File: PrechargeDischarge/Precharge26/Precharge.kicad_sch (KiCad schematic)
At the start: 117 parts, among them J1 MicroFit, J2 Mini-Fit_Jr_5566-04A, J3 Micro-Fit 43045-0212, K1 OMRON-G2RL-24, K2 G7L-2A-X-L, K3 Relay_SPST-NC, Q1 2N7002, Q2 MMBT3906, Q3 2N7002, Q4 PMOS, U1 TJA1051T-3, U10 LM393, U11 4N35, U2 SPAN02A-12, U3 Teensy4.0, U4 LM1117-5.0, U5 4N35, U6 4N35, U7 LM331, U8 LM331, U9 LM2904

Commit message: Precharge
Fixed Ground plane distance, added new DC converter, fixed precharge resistor value
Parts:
- R46: value HSA25390RJ -> HSA253K3J
- R51: footprint (none) -> Resistor_SMD:R_1206_3216Metric
- U2: footprint Precharge:SPAN02 -> Precharge:DC-DCSPAN02W8-12
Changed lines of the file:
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@@
 			"AEQAcgA0AGkAaQBXAEwAMwBlAFEAMgBSADQAQgBKAHQATQB5AGgAbABGAFIAcQBsAEMAbwBjAEEA"
 			"QwBQAHAALwBQAGEARABRAEsAZwBuAEQAeAA0AHMAWABTADAAbABMAGsAbQBBAEwAWABPAFgAUgA3"
-			"AG4AZQBGAHcATwBJAHEATABpAC8AMQArAFAAegBRAC8AZAByADEAQwAxAGQAaA=="
+			"AG4AZQBGAHcATwBJAHEATABpAC8AMQArAFAAegBRAC8AZAByADEAQwAxAGQAaABEADMASABPAHEA"
+			"QgBZAEYAQQBBAE8ASAB2AE0AMgBmAE8ASgBDAFEAawBEAEIANAA4AHUARgBlAHYAWABxAEkAbwBH"
+			"AG8AMQBHAHgASwA5AGgANABvAGcAMAB1ACsAcgBhAGEASAAwAEIAbQBlAEIAbwBOAEIAcgBvAGYA"
+			"eQBoAFgAKwB1AHkAegB6ACsAYgBNAG0AUwBPAEsAbwBzAGYAagBPAFgAcgAwADYAQgBOAFAAUABC"
+			"AEUAVABFADEATwBOAHgAQQA2ADAAcABxAFMAawBKAEIAZwBNAHkAbABYAG4AeABoAGEAaQBsAFMA"
+			"UQBwAE8AVABuAFoAWQBEAEMAMABhAHQAWABLAFkAcgBFAEkAZwByAEIALwAvAC8ANQBWAHEAMQBi"
+			"AGwANQBPAFEARQBnADgARwBSAEkAMABkAE8AbQBEAEEAQgBoAFYAegB2AHYALwA5ACsAUQBrAEwA"
+			"QwBMAGIAZgBjAFkAagBRAGEAVgA2ADUAYwBHAFIATQBUAE0AMgBUAEkAawBNADIAYgBOACsALwBl"
+			"AHYAUgB2AFAAagBpAEEASQBCAG8ATgBoADcATgBpAHgAVgBxAHMAVgBmAHEAaQAxAGYAWABBAGMA"
+			"agBRADYATgBiAHUAYgBIAHcAYwBGAHgALwBVAEcAeQBpAHIAeAA1AFQAUABXAHUASAA1AFgAUgBV"
+			"AE4AUwB5AHMAcgBLAG0AVABKAGsAeQBiAHQAeQA0AEkAMABlAE8AMABNAGkAcQBWAHEAdQBSAFcA"
+			"TgBZAEkAeAAxAG8AcQBpAEwASABaAGIARgBSADEAegBoAGgAVABxAFYAUwBEAEIAZwAxAGEAdAAy"
+			"ADUAZABjAG4ASgB5AFIAawBZAEcAegBOAEsAcgBsADkAVwBGAFEAcQBHAEwARgB5ADkAQwA2AEsA"
+			"MwAyAC8ASQBUADYAQQBrAEUAUQB4AG8AOABmAGIANwBGAFkAUgBvAHcAWQBFAFIAOABmAGYAKwA3"
+			"AGMAdQBWAG0AegBaAGgAMAA2AGQASwBoAEQAaAB3ADYATQBzAFoAZABmAGYAbgBuADcAOQB1ADAA"
+			"NABNADYAdABXAHIAZABxAHcAWQBZAFAASAA0ADUARQBrAGEAZQBYAEsAbABkADkAKwArACsAMgA1"
+			"AGMAKwBkAE8AbgB6ADYAZABrADUAUAB6AHcAUQBjAGYATABGADIANgA5AEsATwBQAFAAdABxAHkA"
+			"WgBZAHYAUAA1ADQAUABvAGkATQBsAFMAYgBSADgAZgBSACsATQBDAEoANAA0AGMASABCAHcAMQBE"
+			"AGoAQQBWAHAAVgBLAEoAVQBEAFgAVgBvADEAUQBYAHcASABXAGcAYQBQAHIAOQ=="
 		)
 	)
@@
 			)
 		)
-		(property "Footprint" "Precharge:SPAN02"
+		(property "Footprint" "Precharge:DC-DCSPAN02W8-12"
 			(at 62.23 135.89 0)
 			(effects
@@
 			)
 		)
-		(property "Value" "HSA25390RJ"
+		(property "Value" "HSA253K3J"
 			(at 63.5 213.36 90)
 			(effects
@@
 			)
 		)
-		(property "Footprint" ""
+		(property "Footprint" "Resistor_SMD:R_1206_3216Metric"
 			(at 65.786 45.974 90)
 			(effects

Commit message: added discharge relay and resistor footprints to precharge board
still need all part numbers but ffootprints are selected, go shopping on JLC
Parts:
- removed K3: Relay_SPST-NC, Library:Relay_SPST_NC_COMUS, symbol Relay:Relay_SPST-NC
- removed Q4: PMOS, Package_TO_SOT_THT:TO-220-3_Vertical, symbol Simulation_SPICE:PMOS
- added D13: D, Diode_SMD:D_SMA, symbol Device:D
- added H1: MountingHole, MountingHole:MountingHole_3.2mm_M3, symbol Mechanical:MountingHole
- added H2: MountingHole, symbol Mechanical:MountingHole
- added J4: Micro-Fit 43045-0212, Connector_Molex:Molex_Micro-Fit_3.0_43045-0212_2x01_P3.00mm_Vertical, symbol Connector:Conn_01x02_Pin
- added K4: Relay_SPST-NC, Precharge:Discharge_relay, symbol Relay:SANYOU_SRD_Form_C
- added Q5: NMOS, Package_TO_SOT_SMD:SOT-23, symbol Simulation_SPICE:NMOS
- J1: symbol Connector:Conn_01x08_Female -> Connector:Conn_01x08_Pin
- J2: symbol Connector:Conn_01x04_Female -> Connector:Conn_01x04_Pin
- J3: symbol Connector:Conn_01x02_Female -> Connector:Conn_01x02_Pin
- R50: value 3k -> HSA503K0J; footprint (none) -> Precharge:Discharge_Resistor
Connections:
- net SHUTDOWN is gone; now on net GLV+: R51.1
- net +12V: now also D13.1 (K), K4.2
- net CANH: now also J1.8 (Pin_8)
- net CANL: now also J1.7 (Pin_7)
- net GLV+: now also J1.1 (Pin_1), Q5.2 (G)
- net GLV-: now also J1.5 (Pin_5), Q5.3 (S)
- net PDOC_OK: now also J1.6 (Pin_6)
- net PRECH_STS: now also J1.4 (Pin_4)
- net SHTDN_OUT: now also J1.3 (Pin_3)
- net TS-: now also J3.1 (Pin_1), J3.2 (Pin_2)
- net VinTS: now also J2.4 (Pin_4)
- net at K2.8: now also J2.1 (Pin_1)
- net at R50.1: now also K4.4
- net HV_OUT renamed MSD_IN
- net MSD_IN: now also J4.2 (Pin_2)
- new net: D13.2 (A), K4.5, Q5.1 (D)
- new net IR+_MC: J4.1 (Pin_1), K4.1
- no-connect marks 9 -> 12
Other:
- note added: "voltage of the shutdown circuit. 12V when on, 0V when off, want discharge to be open when shutdown circuit is 12V"
- note removed: "SHUTDOWN is the voltage of the shutdown circui. 12V when on, 0V when off"
- moved on the sheet: R51

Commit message: precharge
fixed board edges
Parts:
- K1: JLC (none) -> C1524522; MFR (none) -> G2RL-24 DC12

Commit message: precharge/discharge. charging
removed discharge ffrom precharge and put it on board out of battery, updqted charging according to discharge
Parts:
- removed H1: MountingHole, MountingHole:MountingHole_3.2mm_M3, symbol Mechanical:MountingHole
- removed H2: MountingHole, symbol Mechanical:MountingHole
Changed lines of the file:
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@@
 	(text_box "PRECHARGE"
 		(exclude_from_sim no)
-		(at 11.43 111.76 0)
+		(at -132.08 170.18 0)
 		(size 426.72 289.56)
 		(margins 0.9525 0.9525 0.9525 0.9525)
@@
 				)
 				(justify left)
+				(hide yes)
 			)
 		)
@@
 				)
 				(justify left)
+				(hide yes)
 			)
 		)
@@
 					(size 1.27 1.27)
 				)
+				(hide yes)
 			)
 		)
@@
 	)
 	(symbol
-		(lib_id "Mechanical:MountingHole")
-		(at 472.44 226.06 0)
-		(unit 1)
-		(exclude_from_sim no)
-		(in_bom no)
-		(on_board yes)
-		(dnp no)
-		(fields_autoplaced yes)
-		(property "Reference" "H2"
-			(at 474.98 224.7899 0)
-			(effects
-				(font
-					(size 1.27 1.27)
-				)
-				(justify left)
-			)
-		)
-		(property "Value" "MountingHole"
-			(at 474.98 227.3299 0)
-			(effects
-				(font
-					(size 1.27 1.27)
-				)
-				(justify left)
-			)
-		)
-		(property "Footprint" ""
-			(at 472.44 226.06 0)
-			(effects
-				(font
-					(size 1.27 1.27)
-				)
-				(hide yes)
-			)
-		)
-		(property "Datasheet" "~"
-			(at 472.44 226.06 0)
-			(effects
-				(font
-					(size 1.27 1.27)
-				)
-				(hide yes)
-			)
-		)
-		(property "Description" "Mounting Hole without connection"
-			(at 472.44 226.06 0)
-			(effects
-				(font
-					(size 1.27 1.27)
-				)
-				(hide yes)
-			)
-		)
-		(property "JLC" ""
-			(at 472.44 226.06 0)
-			(effects
-				(font
-					(size 1.27 1.27)
-				)
-				(hide yes)
-			)
-		)
-		(property "MFR" ""
-			(at 472.44 226.06 0)
-			(effects
-				(font
-					(size 1.27 1.27)
-				)
-				(hide yes)
-			)
-		)
-		(instances
-			(project "Precharge"
-				(path "/56395b7f-8d0b-4695-8aad-21fefa44f8f8"
-					(reference "H2")
-					(unit 1)
-				)
-			)
-		)
-	)
-	(symbol
 		(lib_id "Simulation_SPICE:NMOS")
 		(at 101.6 59.69 90)
@@
 					(unit 1)
 				)
-			)
-		)
-	)
-	(symbol
-		(lib_id "Mechanical:MountingHole")
-		(at 472.44 218.44 0)
-		(unit 1)
-		(exclude_from_sim no)
-		(in_bom no)
-		(on_board yes)
-		(dnp no)
-		(fields_autoplaced yes)
-		(property "Reference" "H1"
-			(at 474.98 217.1699 0)
-			(effects
-				(font
-					(size 1.27 1.27)
-				)
-				(justify left)
-			)
-		)
-		(property "Value" "MountingHole"
-			(at 474.98 219.7099 0)
-			(effects
-				(font
-					(size 1.27 1.27)
-				)
-				(justify left)
-			)
-		)
-		(property "Footprint" "MountingHole:MountingHole_3.2mm_M3"
-			(at 472.44 218.44 0)
-			(effects
-				(font
-					(size 1.27 1.27)
-				)
-				(hide yes)
-			)
-		)
-		(property "Datasheet" "~"
-			(at 472.44 218.44 0)
-			(effects
-				(font
-					(size 1.27 1.27)
-				)
-				(hide yes)
-			)
-		)
-		(property "Description" "Mounting Hole without connection"
-			(at 472.44 218.44 0)
-			(effects
-				(font
-					(size 1.27 1.27)
-				)
-				(hide yes)
-			)
-		)
-		(property "JLC" ""
-			(at 472.44 218.44 0)
-			(effects
-				(font
-					(size 1.27 1.27)
-				)
-				(hide yes)
-			)
-		)
-		(property "MFR" ""
-			(at 472.44 218.44 0)
-			(effects
-				(font
-					(size 1.27 1.27)
-				)
-				(hide yes)
-			)
-		)
-		(instances
-			(project ""
-				(path "/56395b7f-8d0b-4695-8aad-21fefa44f8f8"
-					(reference "H1")
-					(unit 1)
-				)

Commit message: Molex Microfit
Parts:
- removed J3: Micro-Fit 43045-0212, Connector_Molex:Molex_Micro-Fit_3.0_43045-0212_2x01_P3.00mm_Vertical, symbol Connector:Conn_01x02_Pin
- added J3: 447690401, Precharge:MICROFIT-4PIN, symbol precharge-lib 2:447690401
- J2: footprint Mini-Fit-Jr-4.20mm-pitch:Molex-Mini-Fit-Jr-4-pin-P4.2mm-RowP4.2mm -> Precharge:MICROFIT-4PIN
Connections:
- net TS-: now also J3.1, J3.2
- no-connect marks 12 -> 14
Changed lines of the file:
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@@
 	)
 	(no_connect
+		(at 270.51 322.58)
+	)
+	(no_connect
 		(at 36.83 229.87)
 	)
@@
 	)
 	(no_connect
+		(at 270.51 325.12)
+	)
+	(no_connect
 		(at 27.94 162.56)
 	)
@@
 			"AGMAKwBkAE8AbgB6ADYAZABrADUAUAB6AHcAUQBjAGYATABGADIANgA5AEsATwBQAFAAdABxAHkA"
 			"WgBZAHYAUAA1ADQAUABvAGkATQBsAFMAYgBSADgAZgBSACsATQBDAEoANAA0AGMASABCAHcAMQBE"
-			"AGoAQQBWAHAAVgBLAEoAVQBEAFgAVgBvADEAUQBYAHcASABXAGcAYQBQAHIAOQ=="
+			"AGoAQQBWAHAAVgBLAEoAVQBEAFgAVgBvADEAUQBYAHcASABXAGcAYQBQAHIAOf/Qxaz/0MWs/9DF"
+			"rP/Qxaz/0MWs/9DFrP/Qxaz/0MWs/9DFrP/Qxaz/0MWs/9DFrP/Qxaz/0MWs/9DFrP/Qxaz/0MWs"
+			"/9DFrP/Qxaz/0MWs/9DFrP/Qxaz/0MWs/9DFrP/Qxaz/0MWs/9DFrP/Qxaz/0MWs/9DFrP/Qxaz/"
+			"0MWs/9DFrP/Qxaz/0MWs/9DFrP/Qxaz/0MWs/9DFrP/Qxaz/0MWs/9DFrP/Qxaz/0MWs/9DFrP/Q"
+			"xaz/0MWs/9DFrP/Qxaz/0MWs/9DFrP/Qxaz/0MWs/9DFrP/Qxaz/0MWs/9DFrP9+enL/VFRU/1RU"
+			"VP9UVFT/VFRU/1RUVP9UVFT/VFRU/1RUVP9UVFT/VFRU/9DFrP/Qxaz/0MWs/9DFrP/Qxaz/0MWs"
+			"/9DFrP/Qxaz/0MWs/9DFrP/Qxaz/0MWs/9DFrP/Qxaz/0MWs/9DFrP/Qxaz/0MWs/9DFrP/Qxaz/"
+			"0MWs/9DFrP/Qxaz/0MWs/9DFrP/Qxaz/0MWs/9DFrP/Qxaz/0MWs/9DFrP/Qxaz/0MWs/9DFrP/Q"
+			"xaz/0MWs/9DFrP/Qxaz/0MWs/9DFrP/Qxaz/0MWs/9DFrP/Qxaz/0MWs/9DFrP/Qxaz/0MWs/9DF"
+			"rP/Qxaz/0MWs/9DFrP/Qxaz/0MWs/9DFrP/Qxaz/0MWs/9DFrP/Qxaz/0MWs/9DFrP/Qxaz/0MWs"
+			"/9DFrP/Qxaz/0MWs/9DFrP/Qxaz/0MWs/9DFrP/Qxaz/0MWs/9DFrP/Qxaz/0MWs/9DFrP/Qxaz/"
+			"0MWs/9DFrP/Qxaz/0MWs/9DFrP/Qxaz/0MWs/9DFrP/Qxaz/0MWs/9DFrP/Qxaz/0MWs/9DFrP/Q"
+			"xaz/0MWs/9DFrP/Qxaz/0MWs/9DFrP/Qxaz/0MWs/9DFrP/Qxaz/0MWs/9DFrP/Qxaz/0MWs/9DF"
+			"rP/Qxaz/0MWs/9DFrP/Qxaz/0MWs/9DFrP/Qxaz/0MWs/9DFrP/Qxaz/0MWs/9DFrP/Qxaz/0MKq"
+			"NgAAAAAAAAAAAAAAAAAAAAAAAAAAAAAAAAAAAAAAAAAAAAAAAAAAAAAAAAAAAAAAAAAAAAAAAAAA"
+			"AAAAAAAAAAAAAAAAz8SrhdDFrP/Qxaz/0MWs/9DFrP/Qxaz/0MWs/9DFrP/Qxaz/0MWs/9DFrP/Q"
+			"xaz/0MWs/9DFrP/Qxaz/0MWs/9DFrP/Qxaz/0MWs/9DFrP/Qxaz/0MWs/9DFrP/Qxaz/0MWs/9DF"
+			"rP/Qxaz/0MWs/9DFrP/Qxaz/0MWs/9DFrP/Qxaz/0MWs/9DFrP/Qxaz/0MWs/9DFrP/Qxaz/0MWs"
+			"/9DFrP/Qxaz/0MWs/9DFrP/Qxaz/0MWs/9DFrP/Qxaz/0MWs/9DFrP/Qxaz/0A=="
 		)
 	)
@@
 	)
 	(symbol
-		(lib_id "Connector:Conn_01x02_Pin")
-		(at 275.59 317.5 0)
-		(mirror y)
-		(unit 1)
-		(exclude_from_sim no)
-		(in_bom yes)
-		(on_board yes)
-		(dnp no)
-		(property "Reference" "J3"
-			(at 278.3332 312.801 0)
-			(effects
-				(font
-					(size 1.27 1.27)
-				)
-			)
-		)
-		(property "Value" "Micro-Fit 43045-0212"
-			(at 278.3332 315.1124 0)
-			(effects
-				(font
-					(size 1.27 1.27)
-				)
-			)
-		)
-		(property "Footprint" "Connector_Molex:Molex_Micro-Fit_3.0_43045-0212_2x01_P3.00mm_Vertical"
-			(at 275.59 317.5 0)
-			(effects
-				(font
-					(size 1.27 1.27)
-				)
-				(hide yes)
-			)
-		)
-		(property "Datasheet" "~"
-			(at 275.59 317.5 0)
-			(effects
-				(font
-					(size 1.27 1.27)
-				)
-				(hide yes)
-			)
-		)
-		(property "Description" "Generic connector, single row, 01x02, script generated"
-			(at 275.59 317.5 0)
-			(effects
-				(font
-					(size 1.27 1.27)
-				)
-				(hide yes)
-			)
-		)
-		(property "JLC" ""
-			(at 275.59 317.5 0)
-			(effects
-				(font
-					(size 1.27 1.27)
-				)
-				(hide yes)
-			)
-		)
-		(property "MFR" ""
-			(at 275.59 317.5 0)
-			(effects
-				(font
-					(size 1.27 1.27)
-				)
-				(hide yes)
-			)
-		)
-		(pin "1"
-		)
-		(pin "2"
-		)
-		(instances
-			(project ""
-				(path "/56395b7f-8d0b-4695-8aad-21fefa44f8f8"
-					(reference "J3")
-					(unit 1)
-				)
-			)
-		)
-	)
-	(symbol
 		(lib_id "Isolator:4N35")
 		(at 55.88 300.99 0)
@@
 			)
 		)
-		(property "Footprint" "Mini-Fit-Jr-4.20mm-pitch:Molex-Mini-Fit-Jr-4-pin-P4.2mm-RowP4.2mm"
+		(property "Footprint" "Precharge:MICROFIT-4PIN"
 			(at 31.75 229.87 0)
 			(effects
@@
 					(unit 1)
 				)
+			)
+		)
+	)
+	(symbol
+		(lib_id "precharge-lib 2:447690401")
+		(at 270.51 317.5 0)
+		(unit 1)
+		(exclude_from_sim no)
+		(in_bom yes)
+		(on_board yes)
+		(dnp no)
+		(fields_autoplaced yes)
+		(property "Reference" "J3"
+			(at 284.48 320.0399 0)
+			(effects
+				(font
+					(size 1.524 1.524)
+				)
+				(justify left)
+			)
+		)
+		(property "Value" "447690401"
+			(at 284.48 322.5799 0)
+			(effects
+				(font
+					(size 1.524 1.524)
+				)
+				(justify left)
+			)
+		)
+		(property "Footprint" "Precharge:MICROFIT-4PIN"
+			(at 270.51 317.5 0)
+			(effects
+				(font
+					(size 1.27 1.27)
+					(italic yes)
+				)
+				(hide yes)
+			)
+		)
+		(property "Datasheet" "https://www.molex.com/en-us/products/part-detail-pdf/447690401?display=pdf"
+			(at 270.51 317.5 0)
+			(effects
+				(font
+					(size 1.27 1.27)
+					(italic yes)
+				)
+				(hide yes)
+			)
+		)
+		(property "Description" ""
+			(at 270.51 317.5 0)
+			(effects
+				(font
+					(size 1.27 1.27)
+				)
+				(hide yes)
+			)
+		)
+		(pin "4"
+		)
+		(pin "3"
+		)
+		(pin "1"
+		)
+		(pin "2"
+		)
+		(instances
+			(project ""
+				(path "/56395b7f-8d0b-4695-8aad-21fefa44f8f8"
+					(reference "J3")
+					(unit 1)
+				)

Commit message: Precharge Testing
Uploaded precharge testing data, settled on 1.5k ohm resistor to precharge MC around 1s
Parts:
- removed D13: D, Diode_SMD:D_SMA, symbol Device:D
- removed J4: Micro-Fit 43045-0212, Connector_Molex:Molex_Micro-Fit_3.0_43045-0212_2x01_P3.00mm_Vertical, symbol Connector:Conn_01x02_Pin
- removed K4: Relay_SPST-NC, Precharge:Discharge_relay, symbol Relay:SANYOU_SRD_Form_C
- removed Q5: NMOS, Package_TO_SOT_SMD:SOT-23, symbol Simulation_SPICE:NMOS
- removed R50: HSA503K0J, Precharge:Discharge_Resistor, symbol Device:R_US
- removed R51: 10k, Resistor_SMD:R_1206_3216Metric, symbol Device:R_US
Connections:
- no-connect marks 14 -> 13
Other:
- note removed: "voltage of the shutdown circuit. 12V when on, 0V when off, want discharge to be open when shutdown circuit is 12V"

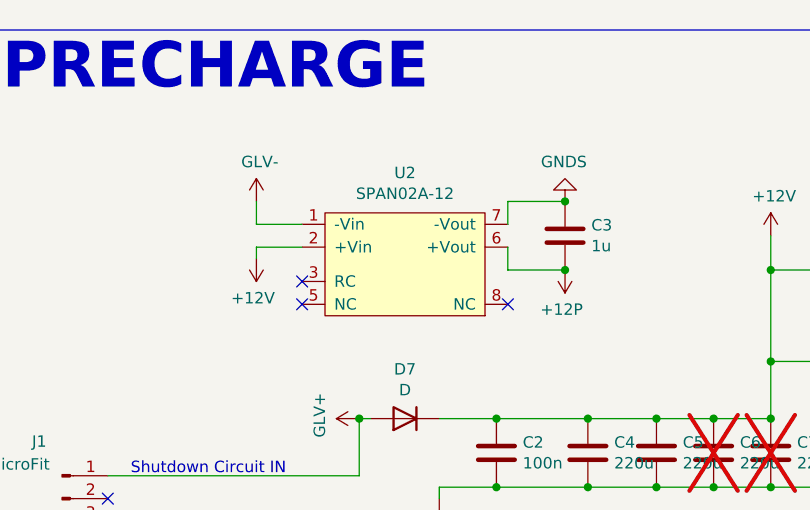
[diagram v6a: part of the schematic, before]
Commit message: precharge dcdc
updated precharge dcdc converter to match footprint
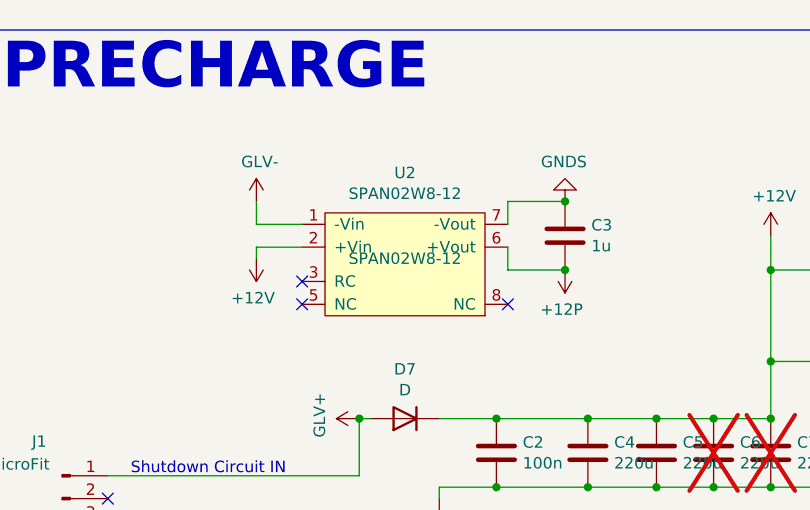
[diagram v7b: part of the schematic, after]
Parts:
- U2: value SPAN02A-12 -> SPAN02W8-12; MFR (none) -> SPAN02W8-12
